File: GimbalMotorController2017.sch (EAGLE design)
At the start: 142 parts, among them J3 APP_2POS_CONFIG5V_HORIZ, Q1 MOSFET-NCHANNELFQP30N06L, Q2 MOSFET-NCHANNELFQP30N06L, Q3 MOSFET-NCHANNELFQP30N06L, Q4 MOSFET-NCHANNELFQP30N06L, Q5 MOSFET-NCHANNELFQP30N06L, Q6 MOSFET-NCHANNELFQP30N06L, Q7 MOSFET-PCHANNEL, Q8 MOSFET-PCHANNEL, Q9 MOSFET-NCHANNELAO3404A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

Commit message: changed power filtering cap count and R26 value for 12v to 3.3v conversion
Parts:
- removed C27, C28, C34, C35, C38, C39: 220u, SparkFun-Passives:CAP_POLPTH4
- removed U$11: TEST_POINT_0.1INDIAM, MRDT-Connectors:TEST_POINT_0.1INDIAM
- added U$3: TEST_POINT_0.1INDIAM, MRDT-Connectors:TEST_POINT_0.1INDIAM
- R26: value 46.4k -> 13.2k
- U$1: device DRV8301:DRV8301 -> MRDT-ICs:DRV8301
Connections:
- new net N$36: C15.+
- new net N$37: U$3.P$1
- net GND: no longer C27.-, C28.-, C34.-, C35.-, C38.-, C39.-
- net PVDD: no longer C15.+, C27.+, C28.+, C34.+, C35.+, C38.+, C39.+, U$11.P$1
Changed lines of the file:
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@@
 <?xml version="1.0" encoding="utf-8"?>
 <!DOCTYPE eagle SYSTEM "eagle.dtd">
-<eagle version="7.3.0">
+<eagle version="8.3.2">
 <drawing>
 <settings>
 <setting alwaysvectorfont="no"/>
+<setting keepoldvectorfont="yes"/>
 <setting verticaltext="up"/>
 </settings>
@@
 </classes>
 <parts>
-<part name="U$1" library="DRV8301" deviceset="DRV8301" device=""/>
+<part name="U$1" library="MRDT-ICs" deviceset="DRV8301" device=""/>
 <part name="R1" library="SparkFun-Passives" deviceset="RESISTOR" device="0805-RES" value="205k"/>
 <part name="R2" library="SparkFun-Passives" deviceset="RESISTOR" device="0805-RES" value="16.2k"/>
@@
 <part name="C30" library="SparkFun-Passives" deviceset="CAP" device="0805" value="0.01u"/>
 <part name="R23" library="SparkFun-Passives" deviceset="RESISTOR" device="0805-RES" value="3.3"/>
-<part name="R26" library="SparkFun-Passives" deviceset="RESISTOR" device="0805-RES" value="46.4k"/>
+<part name="R26" library="SparkFun-Passives" deviceset="RESISTOR" device="0805-RES" value="13.2k"/>
 <part name="R27" library="SparkFun-Passives" deviceset="RESISTOR" device="0805-RES" value="4.99k"/>
 <part name="C31" library="SparkFun-Passives" deviceset="CAP" device="0805" value="0.1u"/>
@@
 <part name="U$7" library="MRDT-Connectors" deviceset="APP" device="PP45_PCB_HORIZ_RIGHT"/>
 <part name="GND27" library="SparkFun-Aesthetics" deviceset="GND" device=""/>
-<part name="C27" library="SparkFun-Passives" deviceset="CAP_POL" device="PTH4" value="220u"/>
-<part name="C28" library="SparkFun-Passives" deviceset="CAP_POL" device="PTH4" value="220u"/>
 <part name="GND28" library="SparkFun-Aesthetics" deviceset="GND" device=""/>
 <part name="U$14" library="Inductor_DR74" deviceset="INDUCTOR_DR74" device="" value="33u"/>
@@
 <part name="R13" library="SparkFun-Passives" deviceset="RESISTOR" device="1206" value=".001"/>
 <part name="R18" library="SparkFun-Passives" deviceset="RESISTOR" device="1206" value=".001"/>
-<part name="C34" library="SparkFun-Passives" deviceset="CAP_POL" device="PTH4" value="220u"/>
-<part name="C35" library="SparkFun-Passives" deviceset="CAP_POL" device="PTH4" value="220u"/>
 <part name="J3" library="MRDT-Connectors" deviceset="APP_2POS_CONFIG" device="5V_HORIZ"/>
-<part name="C38" library="SparkFun-Passives" deviceset="CAP_POL" device="PTH4" value="220u"/>
 <part name="U$4" library="Molex-SL" deviceset="5PIN" device=""/>
 <part name="GND36" library="SparkFun-Aesthetics" deviceset="GND" device=""/>
-<part name="C39" library="SparkFun-Passives" deviceset="CAP_POL" device="PTH4" value="220u"/>
 <part name="SH1" library="BLDC_Motor_Controller_2016_Rev1" deviceset="SHORT-H" device="T5"/>
 <part name="SH2" library="BLDC_Motor_Controller_2016_Rev1" deviceset="SHORT-H" device="T5"/>
@@
 <part name="D15" library="SparkFun-DiscreteSemi" deviceset="DIODE-ZENER" device="3.3V" value="15V"/>
 <part name="U$10" library="MRDT-Connectors" deviceset="TEST_POINT_0.1INDIAM" device=""/>
-<part name="U$11" library="MRDT-Connectors" deviceset="TEST_POINT_0.1INDIAM" device=""/>
 <part name="U$12" library="MRDT-Connectors" deviceset="TEST_POINT_0.1INDIAM" device=""/>
 <part name="U$15" library="MRDT-Connectors" deviceset="TEST_POINT_0.1INDIAM" device=""/>
@@
 <part name="GND37" library="SparkFun-Aesthetics" deviceset="GND" device=""/>
 <part name="SUPPLY4" library="SparkFun-Aesthetics" deviceset="VCC" device=""/>
+<part name="U$3" library="MRDT-Connectors" deviceset="TEST_POINT_0.1INDIAM" device=""/>
 </parts>
 <sheets>
@@
 <instance part="U$7" gate="G$1" x="330.2" y="-144.78"/>
 <instance part="GND27" gate="1" x="314.96" y="-114.3"/>
-<instance part="C27" gate="G$1" x="-33.02" y="134.62"/>
-<instance part="C28" gate="G$1" x="-43.18" y="134.62"/>
 <instance part="GND28" gate="1" x="276.86" y="-149.86"/>
 <instance part="U$14" gate="G$1" x="48.26" y="50.8"/>
@@
 <instance part="R13" gate="G$1" x="142.24" y="30.48" rot="R90"/>
 <instance part="R18" gate="G$1" x="142.24" y="-60.96" rot="R90"/>
-<instance part="C34" gate="G$1" x="-53.34" y="134.62"/>
-<instance part="C35" gate="G$1" x="-63.5" y="134.62"/>
 <instance part="J3" gate="GND" x="330.2" y="-111.76"/>
 <instance part="J3" gate="VCC" x="330.2" y="-104.14"/>
-<instance part="C38" gate="G$1" x="-73.66" y="134.62"/>
 <instance part="U$4" gate="G$1" x="325.12" y="-60.96" rot="MR180"/>
 <instance part="GND36" gate="1" x="309.88" y="-63.5" rot="R270"/>
-<instance part="C39" gate="G$1" x="-83.82" y="134.62"/>
 <instance part="SH1" gate="G$1" x="101.6" y="-66.04"/>
 <instance part="SH2" gate="G$1" x="101.6" y="25.4"/>
@@
 <instance part="D15" gate="G$1" x="134.62" y="-137.16" rot="R90"/>
 <instance part="U$10" gate="G$1" x="-78.74" y="86.36"/>
-<instance part="U$11" gate="G$1" x="-12.7" y="142.24"/>
 <instance part="U$12" gate="G$1" x="134.62" y="68.58"/>
 <instance part="U$15" gate="G$1" x="134.62" y="50.8"/>
@@
 <instance part="GND37" gate="1" x="27.94" y="-35.56" rot="R90"/>
 <instance part="SUPPLY4" gate="G$1" x="-45.72" y="-48.26"/>
+<instance part="U$3" gate="G$1" x="-12.7" y="144.78"/>
 </instances>
 <busses>
@@
 <pinref part="C15" gate="G$1" pin="-"/>
 <pinref part="C37" gate="G$1" pin="-"/>
-<pinref part="C27" gate="G$1" pin="-"/>
-<wire x1="-33.02" y1="129.54" x2="-33.02" y2="119.38" width="0.1524" layer="91"/>
-<wire x1="-33.02" y1="119.38" x2="-22.86" y2="119.38" width="0.1524" layer="91"/>
-<junction x="-22.86" y="119.38"/>
-<pinref part="C28" gate="G$1" pin="-"/>
-<wire x1="-43.18" y1="129.54" x2="-43.18" y2="119.38" width="0.1524" layer="91"/>
-<wire x1="-43.18" y1="119.38" x2="-33.02" y2="119.38" width="0.1524" layer="91"/>
-<junction x="-33.02" y="119.38"/>
-<pinref part="C35" gate="G$1" pin="-"/>
-<wire x1="-63.5" y1="129.54" x2="-63.5" y2="119.38" width="0.1524" layer="91"/>
-<wire x1="-63.5" y1="119.38" x2="-53.34" y2="119.38" width="0.1524" layer="91"/>
-<junction x="-43.18" y="119.38"/>
-<pinref part="C34" gate="G$1" pin="-"/>
-<wire x1="-53.34" y1="119.38" x2="-43.18" y2="119.38" width="0.1524" layer="91"/>
-<wire x1="-53.34" y1="129.54" x2="-53.34" y2="119.38" width="0.1524" layer="91"/>
-<junction x="-53.34" y="119.38"/>
-<pinref part="C38" gate="G$1" pin="-"/>
-<wire x1="-73.66" y1="129.54" x2="-73.66" y2="119.38" width="0.1524" layer="91"/>
-<wire x1="-73.66" y1="119.38" x2="-63.5" y2="119.38" width="0.1524" layer="91"/>
-<junction x="-63.5" y="119.38"/>
-<pinref part="C39" gate="G$1" pin="-"/>
-<wire x1="-73.66" y1="119.38" x2="-83.82" y2="119.38" width="0.1524" layer="91"/>
-<wire x1="-83.82" y1="119.38" x2="-83.82" y2="129.54" width="0.1524" layer="91"/>
-<junction x="-73.66" y="119.38"/>
 </segment>
 <segment>
@@
 </segment>
 <segment>
-<wire x1="-22.86" y1="137.16" x2="-22.86" y2="142.24" width="0.1524" layer="91"/>
-<wire x1="-22.86" y1="142.24" x2="-12.7" y2="142.24" width="0.1524" layer="91"/>
-<wire x1="-12.7" y1="142.24" x2="-12.7" y2="137.16" width="0.1524" layer="91"/>
 <pinref part="C29" gate="G$1" pin="1"/>
 <wire x1="0" y1="137.16" x2="0" y2="142.24" width="0.1524" layer="91"/>
-<wire x1="0" y1="142.24" x2="-12.7" y2="142.24" width="0.1524" layer="91"/>
-<junction x="-12.7" y="142.24"/>
 <pinref part="C30" gate="G$1" pin="1"/>
 <wire x1="12.7" y1="142.24" x2="0" y2="142.24" width="0.1524" layer="91"/>
-<junction x="0" y="142.24"/>
 <pinref part="R26" gate="G$1" pin="1"/>
 <wire x1="30.48" y1="142.24" x2="12.7" y2="142.24" width="0.1524" layer="91"/>
 <junction x="12.7" y="142.24"/>
-<wire x1="-22.86" y1="142.24" x2="-22.86" y2="147.32" width="0.1524" layer="91"/>
-<junction x="-22.86" y="142.24"/>
-<label x="-22.86" y="147.32" size="1.778" layer="95" rot="R90" xref="yes"/>
-<pinref part="C15" gate="G$1" pin="+"/>
+<wire x1="0" y1="142.24" x2="-12.7" y2="142.24" width="0.1524" layer="91"/>
+<junction x="0" y="142.24"/>
 <pinref part="C37" gate="G$1" pin="+"/>
-<wire x1="-22.86" y1="142.24" x2="-33.02" y2="142.24" width="0.1524" layer="91"/>
-<pinref part="C27" gate="G$1" pin="+"/>
-<wire x1="-33.02" y1="142.24" x2="-33.02" y2="137.16" width="0.1524" layer="91"/>
-<wire x1="-33.02" y1="142.24" x2="-43.18" y2="142.24" width="0.1524" layer="91"/>
-<junction x="-33.02" y="142.24"/>
-<pinref part="C28" gate="G$1" pin="+"/>
-<wire x1="-43.18" y1="142.24" x2="-43.18" y2="137.16" width="0.1524" layer="91"/>
-<pinref part="C35" gate="G$1" pin="+"/>
-<wire x1="-43.18" y1="142.24" x2="-53.34" y2="142.24" width="0.1524" layer="91"/>
-<wire x1="-53.34" y1="142.24" x2="-63.5" y2="142.24" width="0.1524" layer="91"/>
-<wire x1="-63.5" y1="142.24" x2="-63.5" y2="137.16" width="0.1524" layer="91"/>
-<junction x="-43.18" y="142.24"/>
-<pinref part="C34" gate="G$1" pin="+"/>
-<wire x1="-53.34" y1="137.16" x2="-53.34" y2="142.24" width="0.1524" layer="91"/>
-<junction x="-53.34" y="142.24"/>
-<pinref part="C38" gate="G$1" pin="+"/>
-<wire x1="-63.5" y1="142.24" x2="-73.66" y2="142.24" width="0.1524" layer="91"/>
-<wire x1="-73.66" y1="142.24" x2="-73.66" y2="137.16" width="0.1524" layer="91"/>
-<junction x="-63.5" y="142.24"/>
-<pinref part="C39" gate="G$1" pin="+"/>
-<wire x1="-73.66" y1="142.24" x2="-83.82" y2="142.24" width="0.1524" layer="91"/>
-<wire x1="-83.82" y1="142.24" x2="-83.82" y2="137.16" width="0.1524" layer="91"/>
-<junction x="-73.66" y="142.24"/>
-<pinref part="U$11" gate="G$1" pin="P$1"/>
+<wire x1="-22.86" y1="142.24" x2="-12.7" y2="142.24" width="0.1524" layer="91"/>
+<wire x1="-12.7" y1="142.24" x2="-12.7" y2="137.16" width="0.1524" layer="91"/>
 </segment>
 <segment>
@@
 </segment>
 </net>
+<net name="N$36" class="0">
+<segment>
+<wire x1="-22.86" y1="137.16" x2="-22.86" y2="147.32" width="0.1524" layer="91"/>
+<pinref part="C15" gate="G$1" pin="+"/>
+<label x="-22.86" y="147.32" size="1.778" layer="95" rot="R90" xref="yes"/>
+</segment>
+</net>
+<net name="N$37" class="0">
+<segment>
+<wire x1="-12.7" y1="139.7" x2="-12.7" y2="144.78" width="0.1524" layer="91"/>
+<junction x="-12.7" y="144.78"/>
+<pinref part="U$3" gate="G$1" pin="P$1"/>
+</segment>
+</net>

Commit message: added CSD18533Q5A fets to Phase C in place of previously used fets
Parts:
- removed Q5, Q6: MOSFET-NCHANNELFQP30N06L, SparkFun-DiscreteSemi:MOSFET-NCHANNELFQP30N06L
- added U3, U4: CSD18533Q5A, CSD18533:CSD18533Q5A
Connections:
- net GND: now also U4.S; no longer Q6.S
- net N$17: now also U3.G; no longer Q5.G
- net N$18: now also U4.G; no longer Q6.G
- net PVDD: now also U3.D; no longer Q5.D
- net SH_C: now also U3.S, U4.D; no longer Q5.S, Q6.D
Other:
- moved on the sheet: C25, C26, D14, D15, R21, R22, R24, R25

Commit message: added CSD18533Q5A fets to Phase B in place of the previously used fets
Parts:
- removed Q3, Q4: MOSFET-NCHANNELFQP30N06L, SparkFun-DiscreteSemi:MOSFET-NCHANNELFQP30N06L
- added U5, U6: CSD18533Q5A, CSD18533:CSD18533Q5A
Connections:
- net N$14: now also U6.G; no longer Q3.G
- net N$15: now also U5.G; no longer Q4.G
- net PVDD: now also U6.D; no longer Q3.D
- net SH_B: now also U5.D, U6.S; no longer Q3.S, Q4.D
- net SL_B: now also U5.S; no longer Q4.S
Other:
- moved on the sheet: C22, C23, C24, D10, D11, R16, R17, R18, R19, R20

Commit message: added CSD18533Q5A fets to Phase A in place of previously used fets. Cleaned up schematic.
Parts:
- removed Q1, Q2: MOSFET-NCHANNELFQP30N06L, SparkFun-DiscreteSemi:MOSFET-NCHANNELFQP30N06L
- added U7, U8: CSD18533Q5A, CSD18533:CSD18533Q5A
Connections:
- net N$13: now also U8.G; no longer Q1.G
- net N$16: now also U7.G; no longer Q2.G
- net PVDD: now also U8.D; no longer Q1.D
- net SH_A: now also U7.D, U8.S; no longer Q1.S, Q2.D
- net SL_A: now also U7.S; no longer Q2.S
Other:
- moved on the sheet: C19, C20, C21, C22, C23, C24, C25, C26, D10, D11, D12, D14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

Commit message: adjusted phase resistor values for 12v to 3.3v voltage divider
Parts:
- R14, R19, R24: value 46.4k -> 13.2k
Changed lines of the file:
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@@
 <part name="GND13" library="SparkFun-Aesthetics" deviceset="GND" device=""/>
 <part name="GND14" library="SparkFun-Aesthetics" deviceset="GND" device=""/>
-<part name="R14" library="SparkFun-Passives" deviceset="RESISTOR" device="0805-RES" value="46.4k"/>
+<part name="R14" library="SparkFun-Passives" deviceset="RESISTOR" device="0805-RES" value="13.2k"/>
 <part name="R15" library="SparkFun-Passives" deviceset="RESISTOR" device="0805-RES" value="4.99k"/>
 <part name="C20" library="SparkFun-Passives" deviceset="CAP" device="0805" value="0.1u"/>
@@
 <part name="GND16" library="SparkFun-Aesthetics" deviceset="GND" device=""/>
 <part name="GND17" library="SparkFun-Aesthetics" deviceset="GND" device=""/>
-<part name="R19" library="SparkFun-Passives" deviceset="RESISTOR" device="0805-RES" value="46.4k"/>
+<part name="R19" library="SparkFun-Passives" deviceset="RESISTOR" device="0805-RES" value="13.2k"/>
 <part name="R20" library="SparkFun-Passives" deviceset="RESISTOR" device="0805-RES" value="4.99k"/>
 <part name="C23" library="SparkFun-Passives" deviceset="CAP" device="0805" value="0.1u"/>
@@
 <part name="GND19" library="SparkFun-Aesthetics" deviceset="GND" device=""/>
 <part name="GND20" library="SparkFun-Aesthetics" deviceset="GND" device=""/>
-<part name="R24" library="SparkFun-Passives" deviceset="RESISTOR" device="0805-RES" value="46.4k"/>
+<part name="R24" library="SparkFun-Passives" deviceset="RESISTOR" device="0805-RES" value="13.2k"/>
 <part name="R25" library="SparkFun-Passives" deviceset="RESISTOR" device="0805-RES" value="4.99k"/>
 <part name="C26" library="SparkFun-Passives" deviceset="CAP" device="0805" value="0.1u"/>

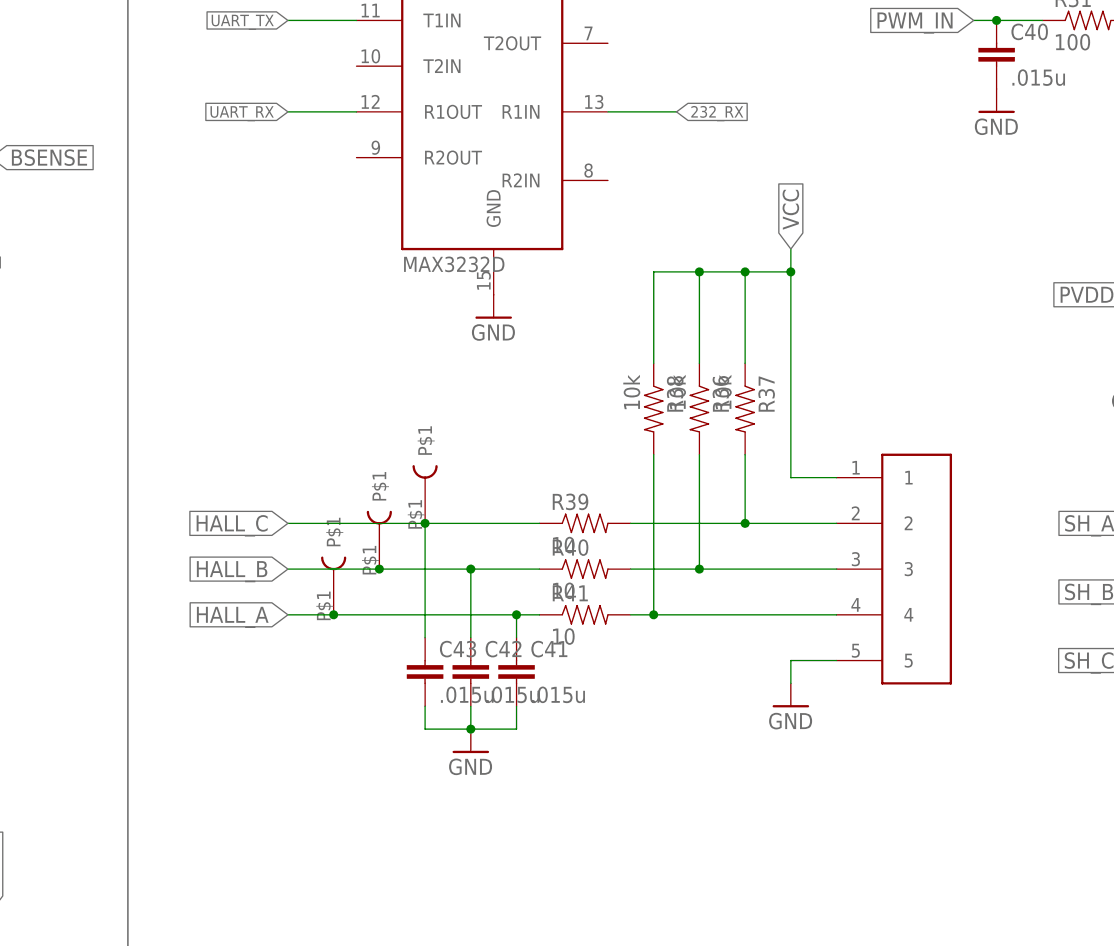
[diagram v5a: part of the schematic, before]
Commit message: removed hall effect sensor connector
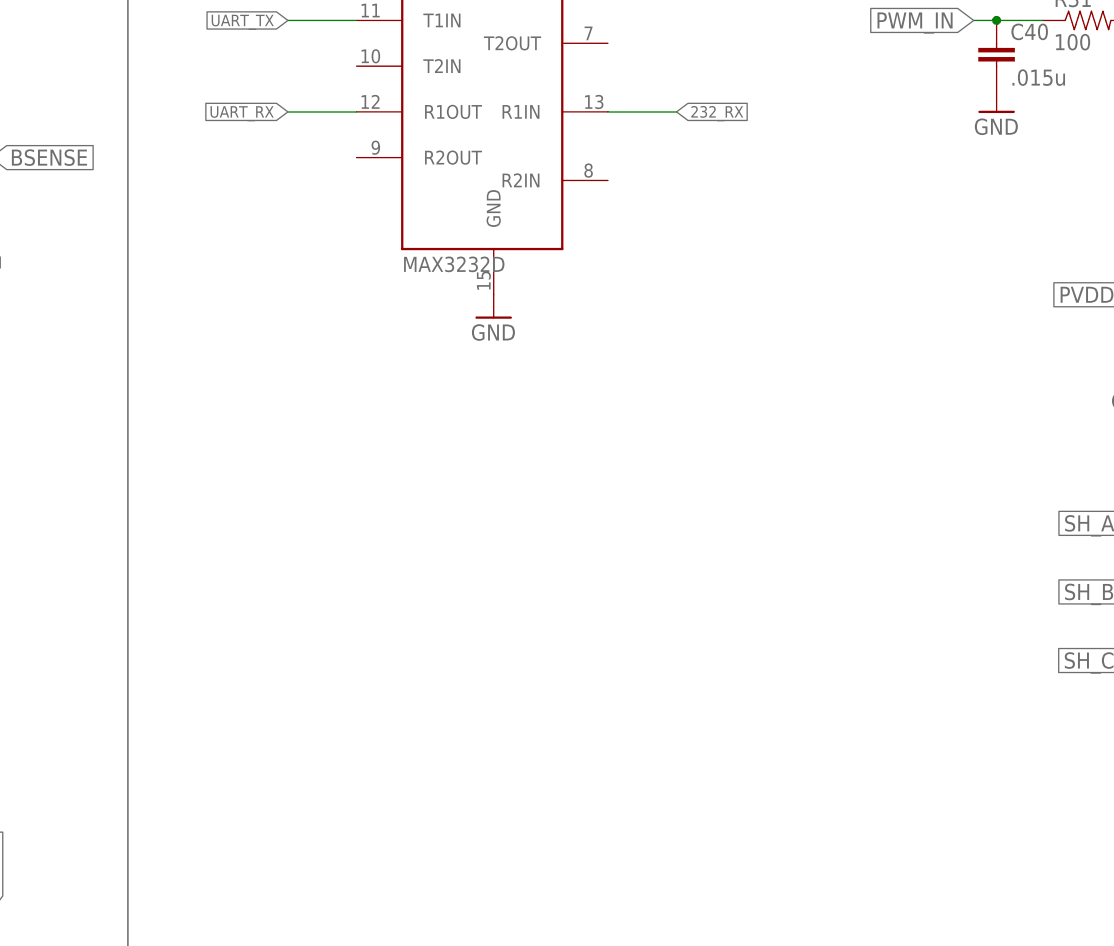
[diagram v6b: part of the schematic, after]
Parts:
- removed C41, C42, C43: .015u, SparkFun-Passives:CAP0805
- removed R36, R37, R38: 10k, SparkFun-Passives:RESISTOR0805-RES
- removed R39, R40, R41: 10, SparkFun-Passives:RESISTOR0805-RES
- removed U$21, U$22, U$23: TEST_POINT_0.1INDIAM, MRDT-Connectors:TEST_POINT_0.1INDIAM
- removed U$8: 5PIN, Molex-SL:5PIN
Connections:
- removed net N$20: R37.2, R39.2, U$8.2
- removed net N$33: R36.2, R40.2, U$8.3
- removed net N$39: R38.2, R41.2, U$8.4
- net GND: no longer C41.2, C42.2, C43.2, U$8.5
- net HALL_A: no longer C41.1, R41.1, U$22.P$1
- net HALL_B: no longer C42.1, R40.1, U$21.P$1
- net HALL_C: no longer C43.1, R39.1, U$23.P$1
- net VCC: no longer R36.1, R37.1, R38.1, U$8.1
